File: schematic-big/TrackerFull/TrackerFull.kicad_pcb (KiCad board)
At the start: 2 copper layers, 43 x 46.9 mm, 51 parts, among them J1 SIM_Card, J2 Conn_01x05_Male, J7 Screw_Terminal_01x02, J8 USB_B_Micro, Q1 IRLML5203, Q2 IRLML5203, Q3 IRLML0030, U1 U.FL, U2 LIS3DSH, U3 MCP73831-2-OT, U5 LP2985-3.3, U6 ATtiny85-20SU

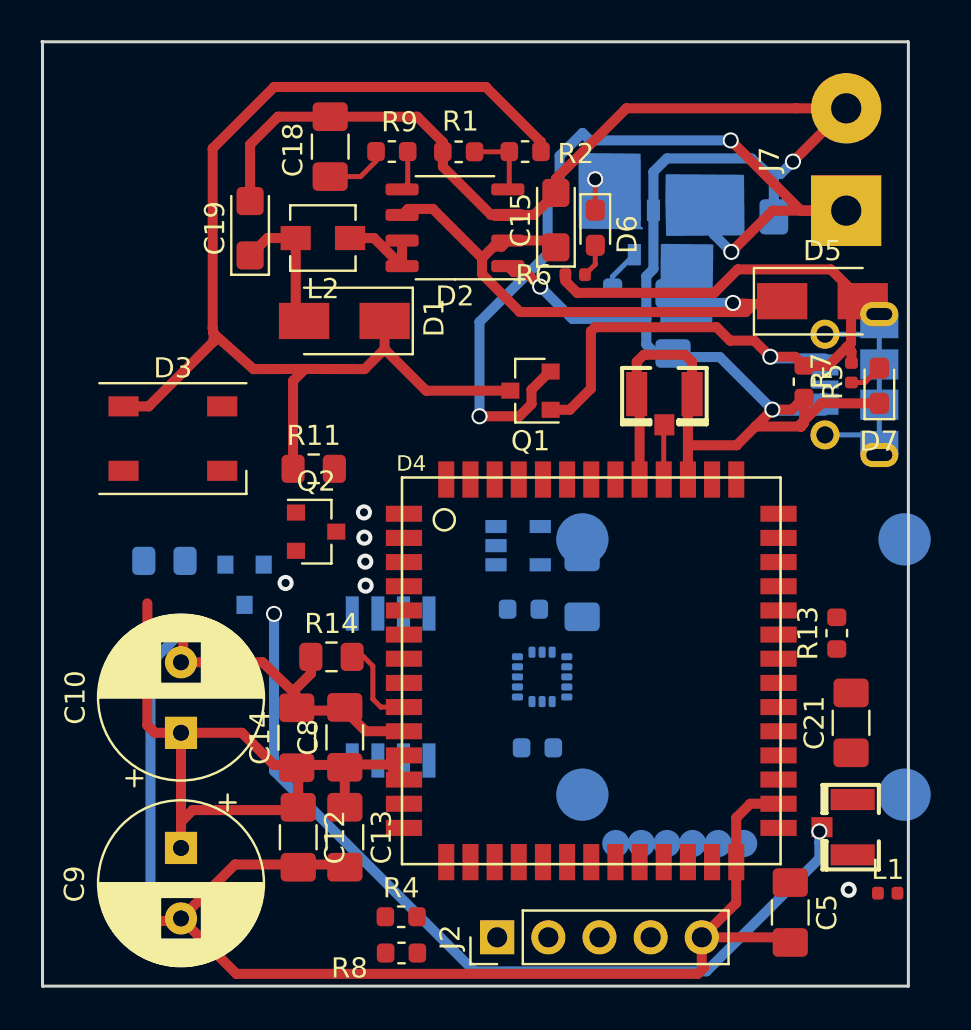
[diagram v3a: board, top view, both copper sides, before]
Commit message: schematic update
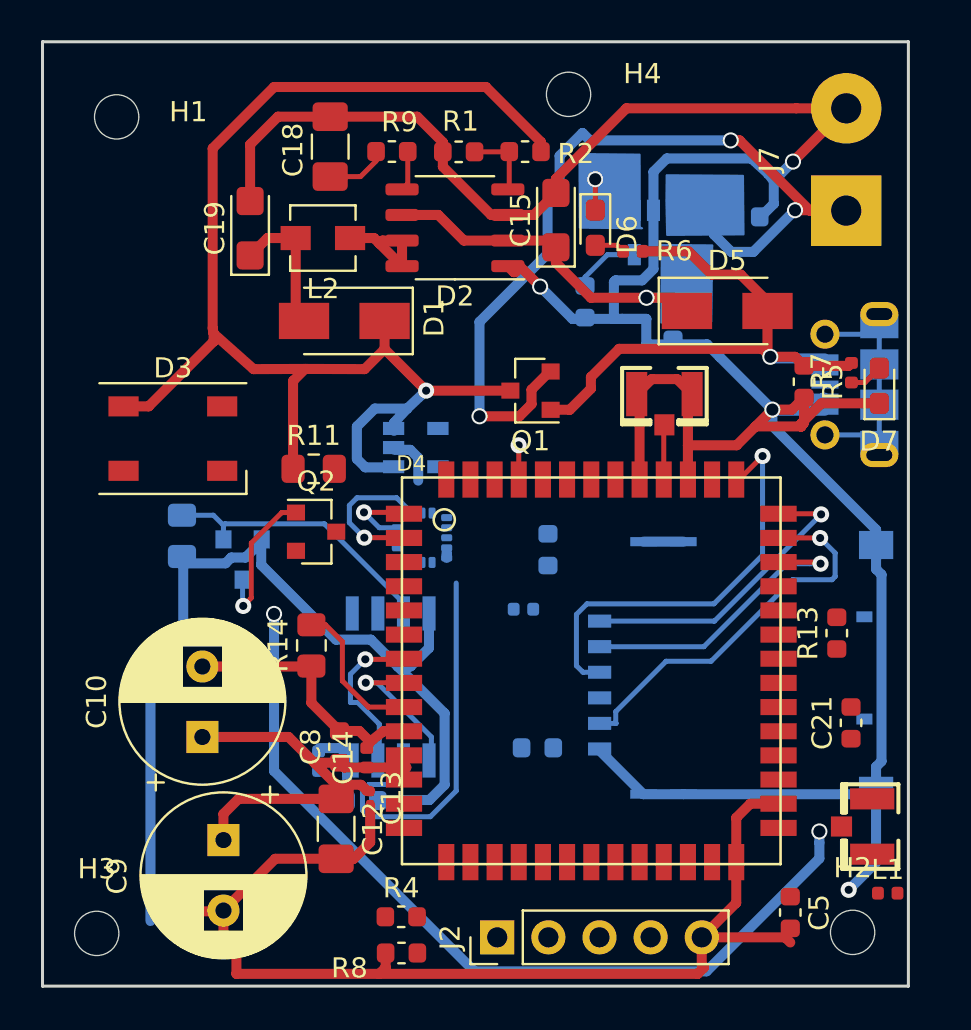
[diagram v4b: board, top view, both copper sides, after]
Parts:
- removed J1: SIM_Card, mailboxNotifier:SIM_SOCKET1
- added C22: 10uF, Capacitor_SMD:C_0603_1608Metric, B.Cu at (101.1, 103.6)
- added C23: 150nF, Capacitor_SMD:C_0402_1005Metric, B.Cu at (98.9, 101.7)
- added H1: MountingHole, MountingHole:MountingHole_2.2mm_M2, F.Cu at (88.9, 69.7)
- added H2: MountingHole, MountingHole:MountingHole_2.2mm_M2, F.Cu at (125.4, 110.2)
- added H3: MountingHole, MountingHole:MountingHole_2.2mm_M2, F.Cu at (87.9, 110.2)
- added H4: MountingHole, MountingHole:MountingHole_2.2mm_M2, F.Cu at (111.3, 68.6)
- added J9: 78646-3001, imported:MOLEX_78646-3001, B.Cu at (120.1, 97.1)
- C13: footprint Capacitor_SMD:C_1206_3216Metric_Pad1.42x1.75mm_HandSolder -> Capacitor_SMD:C_0201_0603Metric
- C14: footprint Capacitor_SMD:C_1206_3216Metric_Pad1.42x1.75mm_HandSolder -> Capacitor_SMD:C_0402_1005Metric
- C2: footprint Capacitor_SMD:C_0603_1608Metric -> Capacitor_SMD:C_0402_1005Metric
- C20, C21, C5, C6, C7, C8: footprint Capacitor_SMD:C_1206_3216Metric_Pad1.42x1.75mm_HandSolder -> Capacitor_SMD:C_0603_1608Metric
- R11: value 100K -> 10K
- moved U2 9.13 mm to (104.0, 90.6), turned to 0 degrees
- moved U5 7.04 mm to (103.7, 86.1)
- moved D5 4.75 mm to (119.2, 79.3)
- moved C14 3.62 mm to (101.3, 101.5)
- moved R6 3.09 mm to (114.5, 76.4), turned to 180 degrees
- moved C20 2.51 mm to (110.3, 91.2)
- moved C13 2.31 mm to (101.5, 103.5)
- moved C9 2.14 mm to (94.2, 105.6)
- moved C12 1.93 mm to (99.8, 105.0)
- moved R10 1.52 mm to (92.1, 90.5), turned to 270 degrees
- moved R3 1.37 mm to (112.1, 78.9)
- moved Q3 1.26 mm to (95.1, 91.7)
- moved R14 1.15 mm to (98.5, 95.9), turned to 90 degrees
- moved C10 1.08 mm to (93.1, 100.5)
- moved U1 0.97 mm to (126.4, 104.9)
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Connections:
- D4 pad 39: (no net) -> /SIM_IO
- D4 pad 40: (no net) -> /VSIM
- D4 pad 41: (no net) -> /SIM_CLK
- D4 pad 42: (no net) -> /SIM_RST
- U6 pad 1: /LED_CTL -> (no net)
- U6 pad 6: (no net) -> /LED_CTL
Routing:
- net GNDREF: track 195.0 -> 272.3 mm
- net /SIM_RST: track 0.00 -> 21.0 mm, vias 0 -> 1
- net /LED_CTL: track 0.00 -> 19.6 mm
- net /VSIM: track 0.00 -> 19.5 mm, vias 0 -> 1
- net /SIM_CLK: track 0.00 -> 15.3 mm, vias 0 -> 1
- net /VBAT: track 39.1 -> 23.8 mm
- net /SIM_IO: track 0.00 -> 14.8 mm, vias 0 -> 1
- net /PWR_CTRL: track 0.00 -> 14.1 mm, vias 1 -> 0
- net BAT_IN: track 57.9 -> 70.3 mm, vias 0 -> 1
- net +5V: track 41.8 -> 29.7 mm
- net /CHARGER_VDD: track 32.1 -> 23.3 mm
- net /IO9: track 0.00 -> 8.04 mm, vias 0 -> 1
- net /ACCEL_SDA: track 0.00 -> 7.46 mm
- net Net-(Q2-Pad1): track 0.00 -> 7.45 mm, vias 0 -> 1
- net /IO8: track 0.00 -> 7.09 mm, vias 0 -> 1
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
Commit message: Last schematic
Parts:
- removed the C14 at (101.3, 101.5)
- removed the C18 at (99.5, 71.2)
- removed C20: 4.7u, Capacitor_SMD:C_0603_1608Metric
- removed C21: 4.7uF, Capacitor_SMD:C_0603_1608Metric
- removed C22: 10uF, Capacitor_SMD:C_0603_1608Metric
- removed the D2 at (105.7, 75.2)
- removed the J2 at (107.8, 110.4)
- removed J8: USB_B_Micro, Connector_USB:USB_Micro-B_Molex-105017-0001
- removed J9: 78646-3001, imported:MOLEX_78646-3001
- removed the R1 at (105.9, 71.4)
- removed the R2 at (109.2, 71.4)
- removed the R3 at (112.1, 78.9)
- removed U6: ATtiny85-20SU, Package_SO:SOIJ-8_5.3x5.3mm_P1.27mm
- added C13: 4.7uF, Capacitor_SMD:C_0603_1608Metric, B.Cu at (182.5, 103.5)
- added C17: 10uF, Capacitor_SMD:C_1206_3216Metric_Pad1.42x1.75mm_HandSolder, B.Cu at (197.9, 83.1)
- added C3: 100nF, Capacitor_SMD:C_0402_1005Metric, F.Cu at (178.4, 83.6)
- added C8: 10pF, Capacitor_SMD:C_0402_1005Metric, F.Cu at (180.8, 93.4)
- added C9: 4.7uF, Capacitor_SMD:C_0603_1608Metric, B.Cu at (178.9, 101.6)
- added D7: D_Schottky, Diode_SMD:D_SMA, B.Cu at (202.6, 87.6)
- added J1: Conn_01x02_Male, Connector_PinHeader_2.54mm:PinHeader_1x02_P2.54mm_Vertical, B.Cu at (186.6, 69.6)
- added J3: AVR-ISP-6, Connector_PinHeader_2.54mm:PinHeader_2x03_P2.54mm_Vertical, B.Cu at (166.9, 80.1)
- added J4: 78646-3001, imported:MOLEX_78646-3001, B.Cu at (198.5, 98.4)
- added J5: Conn_01x02_Male, Connector_PinHeader_2.54mm:PinHeader_1x02_P2.54mm_Vertical, B.Cu at (192.9, 69.6)
- added J6: Screw_Terminal_01x02, Connector_JST:JST_PH_B2B-PH-K_1x02_P2.00mm_Vertical, B.Cu at (193.2, 75.3)
- added R10: 100kOm, Resistor_SMD:R_0603_1608Metric, B.Cu at (189.6, 73.7)
- added R11: 4700, Resistor_SMD:R_0603_1608Metric, F.Cu at (168.5, 83.1)
- added R12: 4700, Resistor_SMD:R_0603_1608Metric, F.Cu at (166.9, 83.1)
- added R15: 250, Resistor_SMD:R_0402_1005Metric, B.Cu at (178.1, 68.0)
- added R16: 100K, Resistor_SMD:R_0603_1608Metric, B.Cu at (182.4, 101.8)
- added R17: 10000, Resistor_SMD:R_0603_1608Metric, B.Cu at (197.4, 86.5)
- added R18: 43000, Resistor_SMD:R_0603_1608Metric, B.Cu at (195.1, 84.7)
- added R19: 10000, Resistor_SMD:R_0603_1608Metric, B.Cu at (191.8, 84.6)
- added R8: 250, Resistor_SMD:R_0402_1005Metric, B.Cu at (196.8, 78.1)
- added SW1: SW_Push, Button_Switch_SMD:SW_Push_1P1T_NO_6x6mm_H9.5mm, F.Cu at (170.7, 98.8)
- added U4: MCP73831-2-OT, Package_TO_SOT_SMD:SOT-23-5, B.Cu at (178.9, 72.7)
- C1: value 10uF -> 4.7u; moved to F.Cu
- C11: renamed from C15; moved to B.Cu
- C15: renamed from C9; footprint Capacitor_THT:CP_Radial_D8.0mm_P3.50mm -> Capacitor_SMD:CP_Elec_8x10.5; moved to B.Cu
- C16: renamed from C10; footprint Capacitor_THT:CP_Radial_D8.0mm_P3.50mm -> Capacitor_SMD:CP_Elec_8x10.5; moved to B.Cu
- C18: renamed from C19; moved to B.Cu
- C2: value 100nF -> 10uF; footprint Capacitor_SMD:C_0402_1005Metric -> Capacitor_SMD:C_0603_1608Metric; moved to F.Cu
- C4: renamed from C23; moved to F.Cu
- C5: value 4.7uF -> 10uF
- D1: value D_Schottky -> A9G; footprint Diode_SMD:D_SMA -> Tracker:A9G2
- D2: renamed from D7; moved to B.Cu
- D3: renamed from D5; moved to B.Cu
- D4: value A9G -> LED; footprint Tracker:A9G2 -> LED_SMD:LED_0603_1608Metric_Pad1.05x0.95mm_HandSolder; moved to B.Cu
- D5: renamed from D3; moved to B.Cu
- D6: value LED -> APW7142; footprint LED_SMD:LED_0603_1608Metric_Pad1.05x0.95mm_HandSolder -> Package_SO:SOP-8_3.9x4.9mm_P1.27mm; moved to B.Cu
- GSM1, L1, L2: moved to B.Cu
- J2: renamed from J7; footprint Connector_Wire:SolderWirePad_1x02_P5.08mm_Drill1.5mm -> Connector_JST:JST_PH_B2B-PH-K_1x02_P2.00mm_Vertical; moved to B.Cu
- Q1: renamed from Q3; moved to F.Cu
- Q3: renamed from Q1; moved to B.Cu
- R1: renamed from R10; moved to F.Cu
- R13: value 100K -> 4700
- R14: value 10K -> 470; footprint Resistor_SMD:R_0805_2012Metric_Pad1.15x1.40mm_HandSolder -> Resistor_SMD:R_0603_1608Metric
- R5: value 100kOm -> 10K
- R6: value 250 -> 10K; footprint Resistor_SMD:R_0402_1005Metric -> Resistor_SMD:R_0603_1608Metric
- R7: value 250 -> 10K; footprint Resistor_SMD:R_0402_1005Metric -> Resistor_SMD:R_0805_2012Metric_Pad1.15x1.40mm_HandSolder
- R9: value 10000 -> 2000; moved to B.Cu
- U1: value U.FL -> LP2985-3.3; footprint mailboxNotifier:U.FL -> Package_TO_SOT_SMD:SOT-23-5
- U2: moved to F.Cu
- U3: value MCP73831-2-OT -> ATtiny85-20SU; footprint Package_TO_SOT_SMD:SOT-23-5 -> Package_SO:SOIJ-8_5.3x5.3mm_P1.27mm; moved to F.Cu
- U5: value LP2985-3.3 -> U.FL; footprint Package_TO_SOT_SMD:SOT-23-5 -> mailboxNotifier:U.FL
- moved C18 110.9 mm to (205.5, 88.8)
- moved L2 100.1 mm to (198.3, 89.3), turned to 0 degrees
- moved D1 93.7 mm to (193.3, 90.0), turned to 0 degrees
- moved D5 93.0 mm to (184.7, 88.4), turned to 180 degrees
- moved H4 89.7 mm to (201.0, 70.7)
- moved R1 86.7 mm to (178.8, 87.3), turned to 90 degrees
- moved U5 85.6 mm to (187.9, 101.4), turned to 90 degrees
- moved C16 83.6 mm to (176.7, 97.1), turned to 180 degrees
- moved C10 81.2 mm to (182.0, 92.8), turned to 90 degrees
- moved H3 81.1 mm to (169.0, 107.7)
- moved C12 80.9 mm to (180.1, 96.0), turned to 180 degrees
- moved D6 80.5 mm to (192.1, 88.4), turned to 0 degrees
- moved H1 80.1 mm to (169.0, 70.7)
- moved C14 79.9 mm to (179.4, 92.9)
- moved R2 79.5 mm to (182.0, 99.8)
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- renumbered C13 to C10, C8 to C14, R4 to R2, R11 to R3, R8 to R4
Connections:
- C1 pad 1: GNDREF -> /3.3v
- C1 pad 2: Net-(C1-Pad2) -> GNDREF
- C2 pad 2: Net-(C1-Pad2) -> /3.3v
- C5 pad 1: /VBAT -> GNDREF
- C5 pad 2: GNDREF -> BAT_IN
- D1 pad 1: BAT_IN -> /ACCEL_CS
- D1 pad 2: /APW_OUT -> /ACCEL_SDO
- D2 pad 2: Net-(D7-Pad2) -> Net-(D2-Pad2)
- D4 pad 1: /ACCEL_SCL -> /CHARGER_STAT
- D4 pad 2: /ACCEL_SDA -> Net-(D4-Pad2)
- D6 pad 1: /CHARGER_STAT -> GNDREF
- D6 pad 2: Net-(D6-Pad2) -> /CHARGER_VDD
- GSM1 pad 3: Net-(D4-Pad45) -> Net-(D1-Pad45)
- R13 pad 1: /VBAT -> /ICSP_SCK
- R13 pad 2: Net-(C21-Pad1) -> /AVR_SCK
- R14 pad 1: GNDREF -> Net-(R14-Pad1)
- R14 pad 2: Net-(D4-Pad9) -> /LED_CTL
- R2 pad 1: /V_BAT -> /VBAT
- R2 pad 2: Net-(D4-Pad15) -> Net-(D1-Pad15)
- R4 pad 1: Net-(D4-Pad15) -> Net-(D1-Pad15)
- R5 pad 1: +5V -> BAT_IN
- R5 pad 2: GNDREF -> /AVR_MOSI_SDA
- R6 pad 1: +5V -> BAT_IN
- R6 pad 2: Net-(D6-Pad2) -> /AVR_SCK
- R7 pad 1: +5V -> GNDREF
- R7 pad 2: Net-(D7-Pad2) -> Net-(D1-Pad9)
- R9 pad 1: Net-(D2-Pad5) -> GNDREF
- R9 pad 2: Net-(C18-Pad2) -> /CHARGER_PROG
- U1 pad 1: GNDREF -> BAT_IN
- U1 pad 3: /GPS_RF -> BAT_IN
- U2 pad 1: Net-(C1-Pad2) -> /3.3v
- U2 pad 14: Net-(C1-Pad2) -> /3.3v
- U2 pad 15: Net-(C1-Pad2) -> /3.3v
- U3 pad 1: /CHARGER_STAT -> /AVR_RST
- U3 pad 2: GNDREF -> Net-(R14-Pad1)
- U3 pad 3: /V_BAT -> /PWR_CTRL
- U3 pad 4: /CHARGER_VDD -> GNDREF
- U3 pad 5: /CHARGER_PROG -> /ICSP_MOSI
- U5 pad 1: BAT_IN -> GNDREF
- U5 pad 3: BAT_IN -> /GPS_RF
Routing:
- net GNDREF: track 272.3 -> 142.9 mm, vias 6 -> 23
- net /HST_RXD: track 0.00 -> 44.0 mm
- net /GPS_RF: track 42.7 -> 0.00 mm, vias 2 -> 0
- net /AVR_RST: track 0.00 -> 42.4 mm, vias 0 -> 1
- net /HST_TXD: track 0.00 -> 38.6 mm
- net /ACCEL_INT1: track 1.70 -> 28.9 mm, vias 1 -> 0
- net BAT_IN: track 70.3 -> 47.5 mm, vias 1 -> 4
- net /SIM_RST: track 21.0 -> 0.00 mm
- net /AVR_MOSI_SDA: track 0.00 -> 20.4 mm, vias 0 -> 2
- net /VSIM: track 19.5 -> 0.00 mm
- net /ICSP_SCK: track 0.00 -> 18.2 mm, vias 0 -> 1
- net /AVR_SCK: track 0.00 -> 17.1 mm, vias 0 -> 2
- net /SIM_CLK: track 15.3 -> 0.00 mm
- net /UART1_RXD: track 0.00 -> 14.8 mm, vias 0 -> 2
- net /SIM_IO: track 14.8 -> 0.00 mm, vias 1 -> 0
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- added copper zone on B.Cu, net /CHARGER_VDD
- added copper zone on B.Cu, net /V_BAT
- added copper zone on B.Cu, net GNDREF

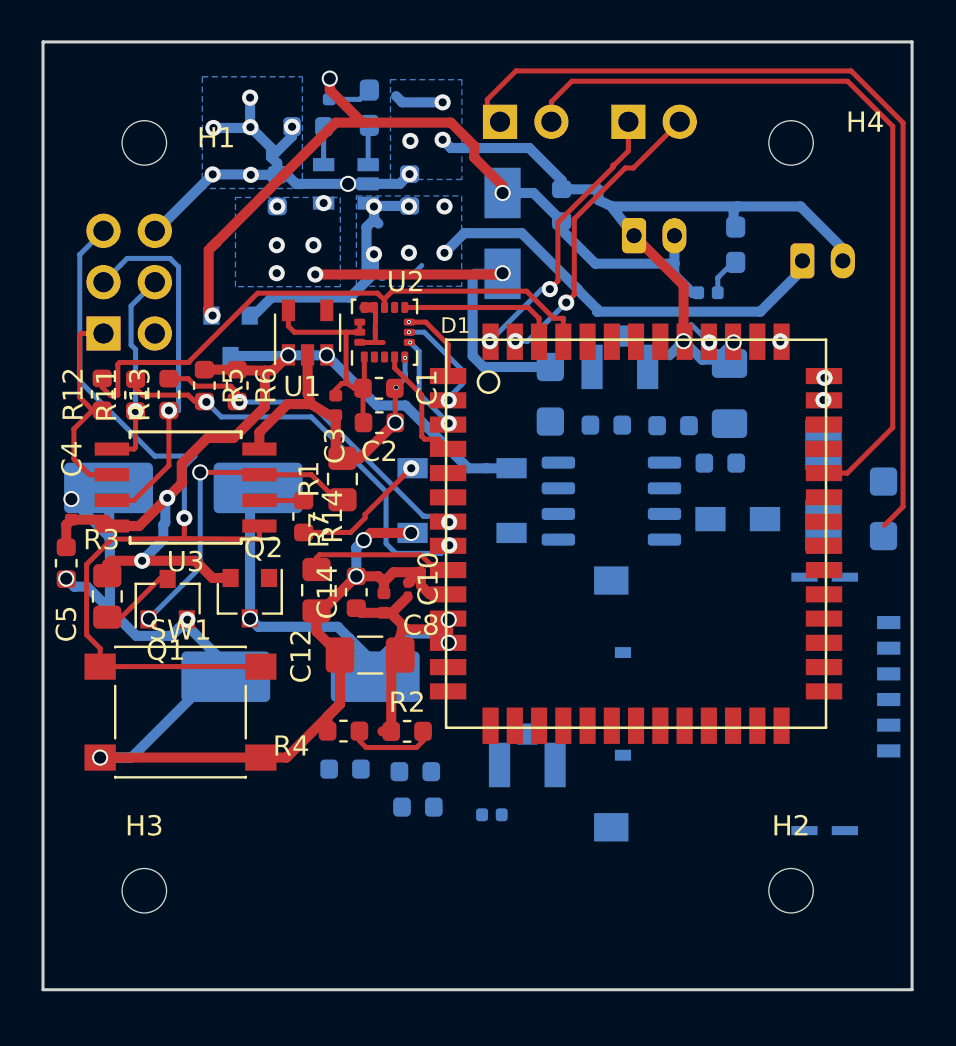
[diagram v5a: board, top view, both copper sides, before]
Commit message: schematic update
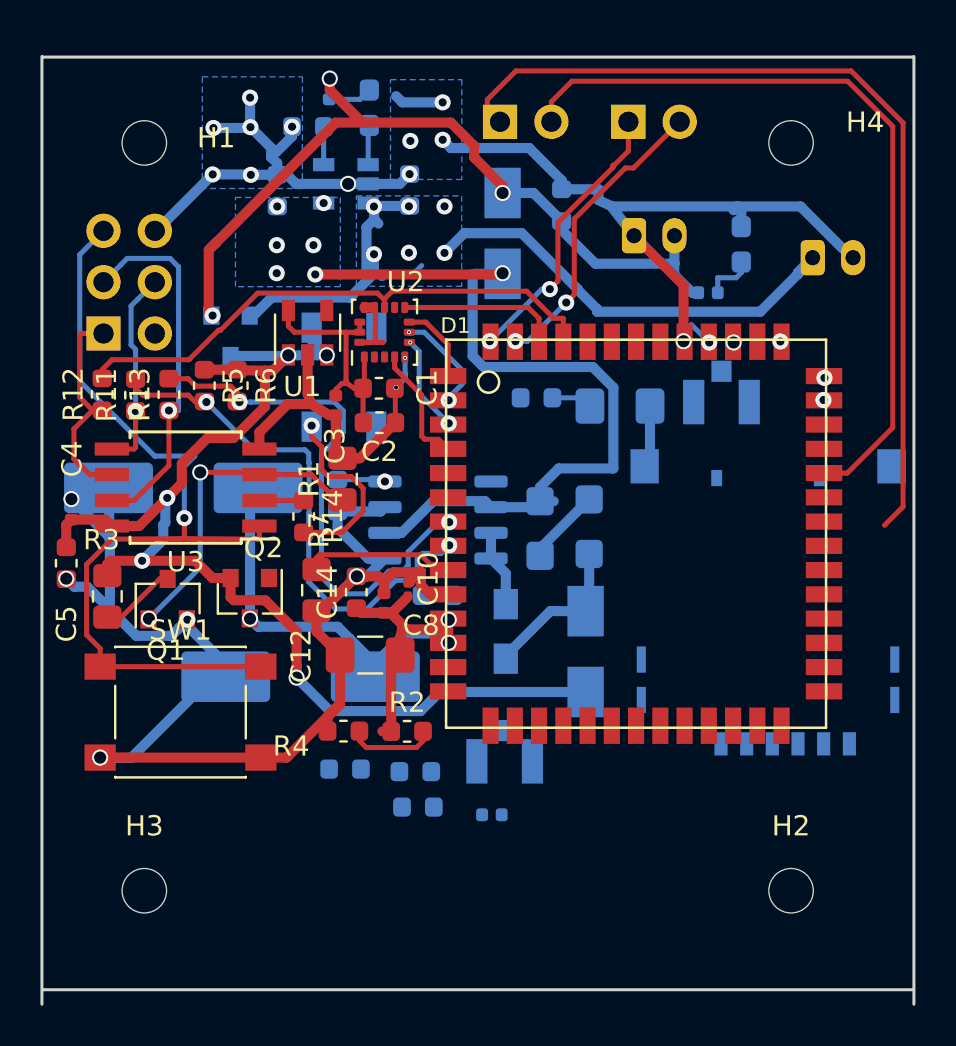
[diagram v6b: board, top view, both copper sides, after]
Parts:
- moved C18 14.6 mm to (191.0, 89.7)
- moved R18 14.4 mm to (183.5, 93.1)
- moved D7 14.4 mm to (190.8, 95.8), turned to 90 degrees
- moved R19 13.7 mm to (178.5, 88.1), turned to 270 degrees
- moved L2 12.8 mm to (186.8, 94.8), turned to 270 degrees
- moved R17 9.65 mm to (188.4, 83.3), turned to 0 degrees
- moved D6 8.63 mm to (183.5, 89.3)
- moved D5 8.45 mm to (178.8, 82.3), turned to 270 degrees
- moved C11 6.66 mm to (188.5, 89.7)
- moved J4 5.48 mm to (199.8, 93.1), turned to 90 degrees
- moved C17 5.46 mm to (192.5, 83.7), turned to 180 degrees
- moved GSM1 5.32 mm to (197.5, 83.5)
- moved U5 1.14 mm to (186.8, 101.3)
- moved J2 0.53 mm to (202.0, 76.3)
- moved D2 0.28 mm to (198.5, 75.7)
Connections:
- D1 pad 18: /AVR_RST -> (no net)
- R18 pad 1: BAT_IN -> /APW_OUT
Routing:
- net /CHARGER_VDD: track 18.9 -> 40.4 mm
- net BAT_IN: track 47.5 -> 60.4 mm, vias 4 -> 5
- net /AVR_SCK: track 17.1 -> 26.9 mm
- net /APW_OUT: track 0.00 -> 7.91 mm
- net GNDREF: track 142.9 -> 149.3 mm, vias 23 -> 20
- net /AVR_MOSI_SDA: track 20.4 -> 25.2 mm
- net /LX: track 0.00 -> 3.83 mm
- net /LED_CTL: track 6.74 -> 9.33 mm
- net Net-(D6-Pad4): track 0.00 -> 2.38 mm, vias 0 -> 1
- net Net-(C17-Pad2): track 0.00 -> 2.02 mm
- net /ACCEL_INT1: track 28.9 -> 27.3 mm
- net /V_BAT: track 35.5 -> 36.2 mm
- net Net-(D2-Pad2): track 1.85 -> 2.54 mm
- net /ACCEL_CS: vias 1 -> 0
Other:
- board size 43 x 46.9 mm -> 43.1 x 46.9 mm

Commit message: latest version. Doesnt work :)
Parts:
- removed H2: MountingHole, MountingHole:MountingHole_2.2mm_M2
- removed the J3 at (166.9, 80.1)
- removed the R11 at (168.5, 83.1)
- removed the R12 at (166.9, 83.1)
- removed the R13 at (170.2, 83.1)
- Q3: moved to F.Cu
- U3: value ATtiny85-20SU -> ATtiny85-20PU; footprint Package_SO:SOIJ-8_5.3x5.3mm_P1.27mm -> Package_DIP:DIP-8_W7.62mm; moved to B.Cu
- moved C5 13.8 mm to (175.9, 82.8), turned to 180 degrees
- moved C9 11.3 mm to (189.8, 104.8)
- moved C13 11.3 mm to (193.4, 106.7)
- moved R13 11.3 mm to (193.3, 105.0)
- moved C4 9.33 mm to (173.2, 83.8), turned to 180 degrees
- moved U3 8.38 mm to (165.4, 81.5), turned to 0 degrees
- moved H3 8.15 mm to (167.5, 99.6)
- moved R5 7.30 mm to (171.1, 75.4), turned to 90 degrees
- moved R3 7.09 mm to (167.0, 86.0)
- moved Q1 7.07 mm to (169.8, 86.2)
- moved Q2 7.07 mm to (173.9, 86.1)
- moved SW1 6.37 mm to (169.3, 92.6)
- moved Q3 4.01 mm to (169.3, 79.4)
- moved R6 3.19 mm to (170.4, 82.1), turned to 180 degrees
- moved R11 2.23 mm to (176.9, 86.9), turned to 90 degrees
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- renumbered J5 to J2, J2 to J3, J6 to J5, R14 to R11, R15 to R12, R16 to R13, R17 to R14, R18 to R15, R19 to R16
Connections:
- U3 pad 5: /ICSP_MOSI -> /AVR_MOSI_SDA
- U3 pad 6: /ICSP_MISO -> /ACCEL_INT1
- U3 pad 7: /ICSP_SCK -> /AVR_SCK
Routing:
- net /AVR_RST: track 42.4 -> 8.76 mm, vias 1 -> 0
- net Net-(R11-Pad1): track 2.20 -> 23.9 mm
- net /ICSP_SCK: track 18.2 -> 0.00 mm, vias 1 -> 0
- net /AVR_MOSI_SDA: track 25.2 -> 41.9 mm, vias 2 -> 1
- net /PWR_CTRL: track 15.9 -> 29.0 mm, vias 2 -> 0
- net /ICSP_MISO: track 10.7 -> 0.00 mm
- net /ICSP_MOSI: track 9.96 -> 0.00 mm, vias 1 -> 0
- net Net-(Q1-Pad3): track 3.77 -> 13.7 mm
- net /AVR_SCK: track 26.9 -> 35.5 mm, vias 2 -> 3
- net /LED_CTL: track 9.33 -> 1.61 mm
- net /ACCEL_INT1: track 27.3 -> 19.9 mm
- net BAT_IN: track 60.4 -> 67.7 mm, vias 5 -> 6
- net GNDREF: track 149.3 -> 142.5 mm, vias 20 -> 18
- net +5V: track 39.3 -> 45.6 mm, vias 3 -> 2
- net /V_BAT: track 36.2 -> 42.2 mm, vias 6 -> 7
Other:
- board size 43.1 x 46.9 mm -> 43.2 x 46.9 mm
